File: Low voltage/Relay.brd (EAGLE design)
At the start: 100 x 80 mm, 9 parts, among them T1 2N1613

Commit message: board layout
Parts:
- removed R1: 1k, resistor:R2012
- moved T1 41.3 mm to (36.8, 22.9), turned to 270 degrees
- moved X2 38.6 mm to (53.6, 35.6)
- moved LED1 37.5 mm to (53.3, 15.8), turned to 90 degrees
- moved D1 35.4 mm to (1.48, 33.0), turned to 268.7 degrees
- moved U$1 32.3 mm to (30.1, 36.6)
- moved U$3 18.3 mm to (38.0, 10.2)
- moved U$4 12.4 mm to (13.5, 8.89)
- moved X1 10.5 mm to (2.54, 17.8)
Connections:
- removed net N$3: LED1.A, R1.2
- net N$2: now also LED1.A; no longer R1.1
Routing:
- net N$8: track 0.00 -> 149.7 mm
- net N$1: track 0.00 -> 106.6 mm
- net GND: track 0.00 -> 104.6 mm
- net N$9: track 0.00 -> 31.0 mm
- net N$2: track 0.00 -> 27.3 mm
- net N$5: track 0.00 -> 19.8 mm
- net N$10: track 0.00 -> 18.1 mm
- net N$7: track 0.00 -> 16.3 mm
- net N$4: track 0.00 -> 7.80 mm
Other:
- board size 100 x 80 mm -> 65 x 49.5 mm

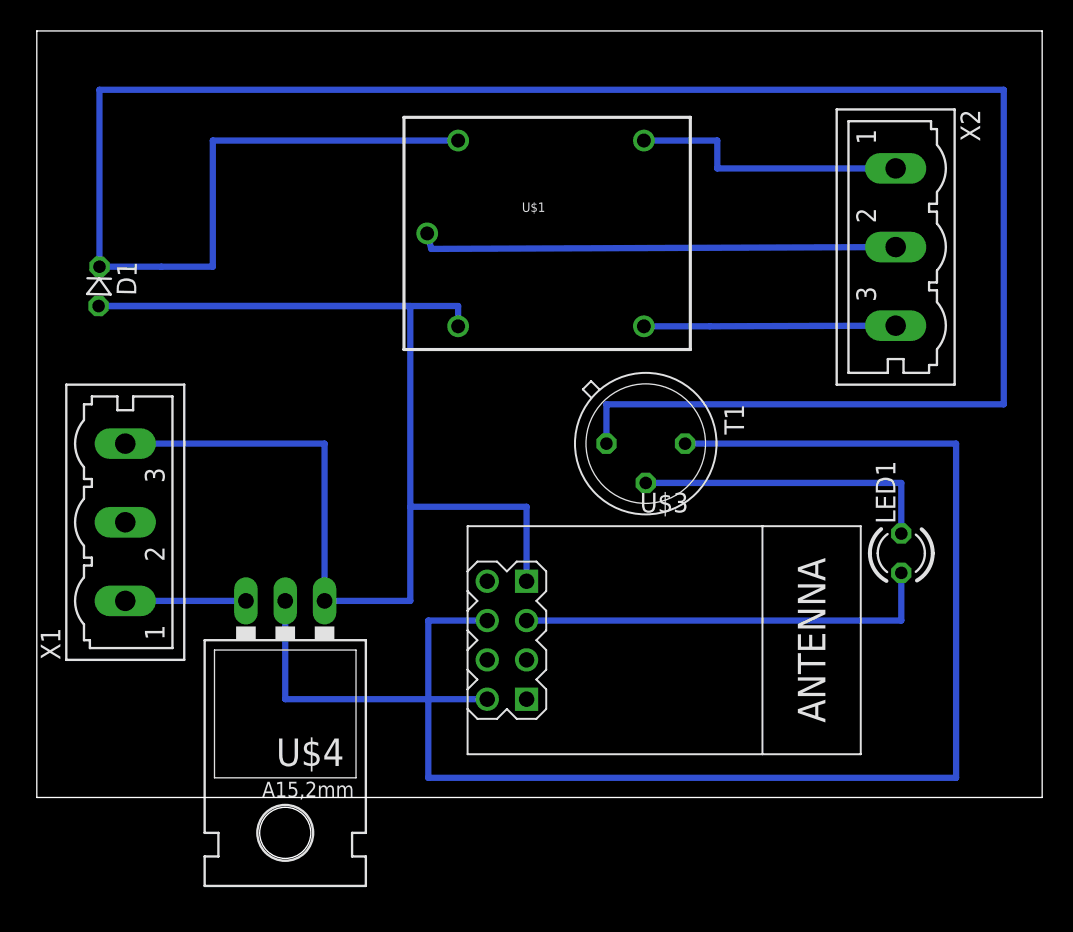
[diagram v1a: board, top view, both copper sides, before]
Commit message: Added board Via
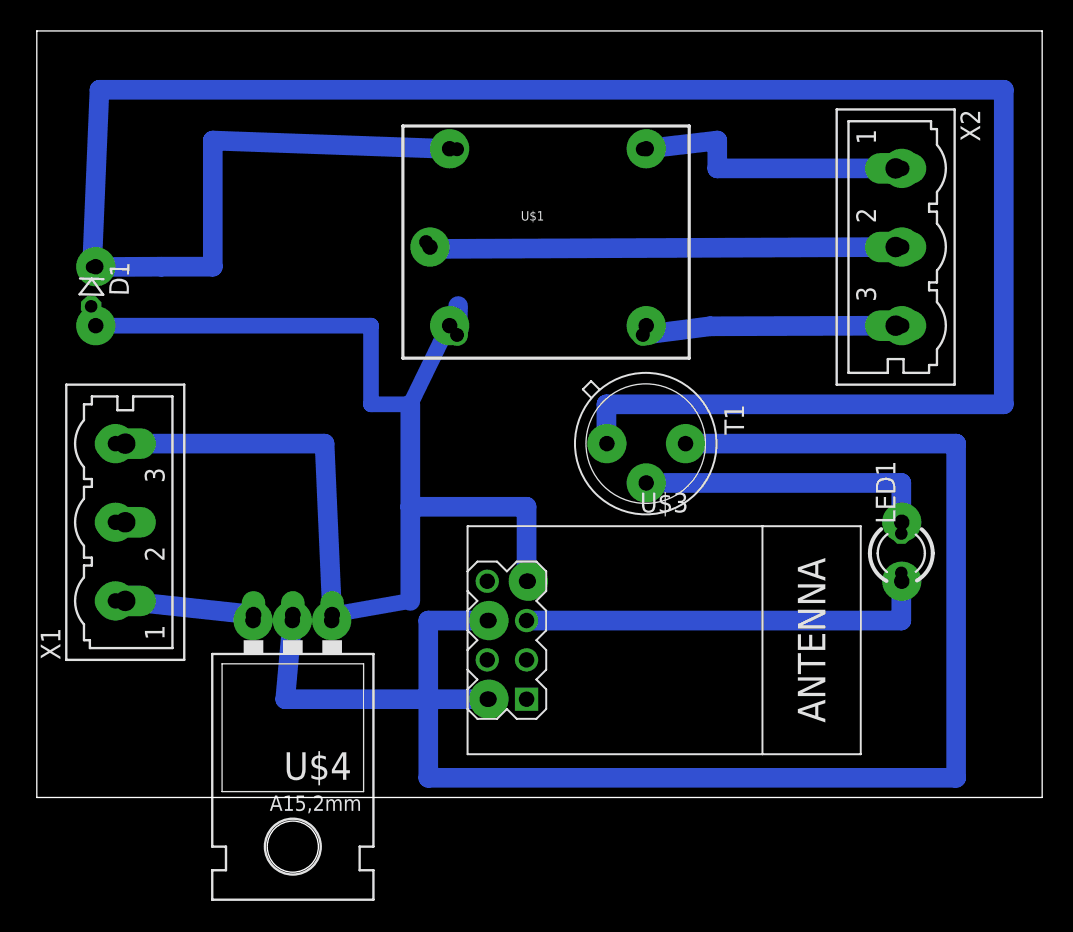
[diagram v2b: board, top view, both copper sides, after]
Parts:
- moved U$4 1.02 mm to (14.0, 8.00)
- moved U$1 0.56 mm to (30.0, 36.0)
- moved D1 0.48 mm to (1.00, 33.0)
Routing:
- net GND: track 104.6 -> 90.0 mm, vias 0 -> 1
- net N$1: track 106.6 -> 105.7 mm, vias 0 -> 1
- net N$4: track 7.80 -> 8.33 mm
- net N$5: vias 0 -> 1
